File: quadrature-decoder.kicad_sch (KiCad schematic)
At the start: 6 parts, among them J1 Screw_Terminal_01x05, J2 Conn_02x20_Counter_Clockwise, U1 4013, U2 4029, U3 4029, U4 4029

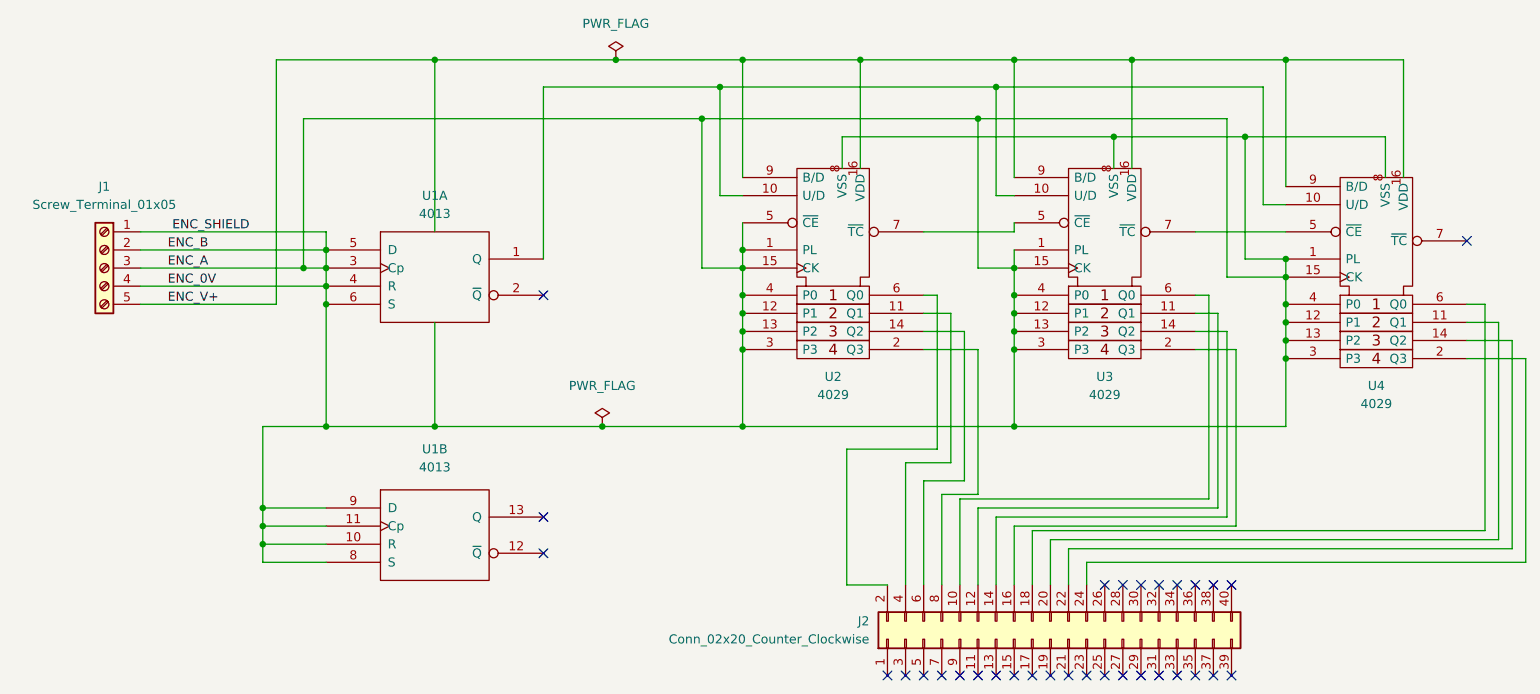
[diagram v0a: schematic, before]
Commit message: Improve routing and component positioning; add capacitors
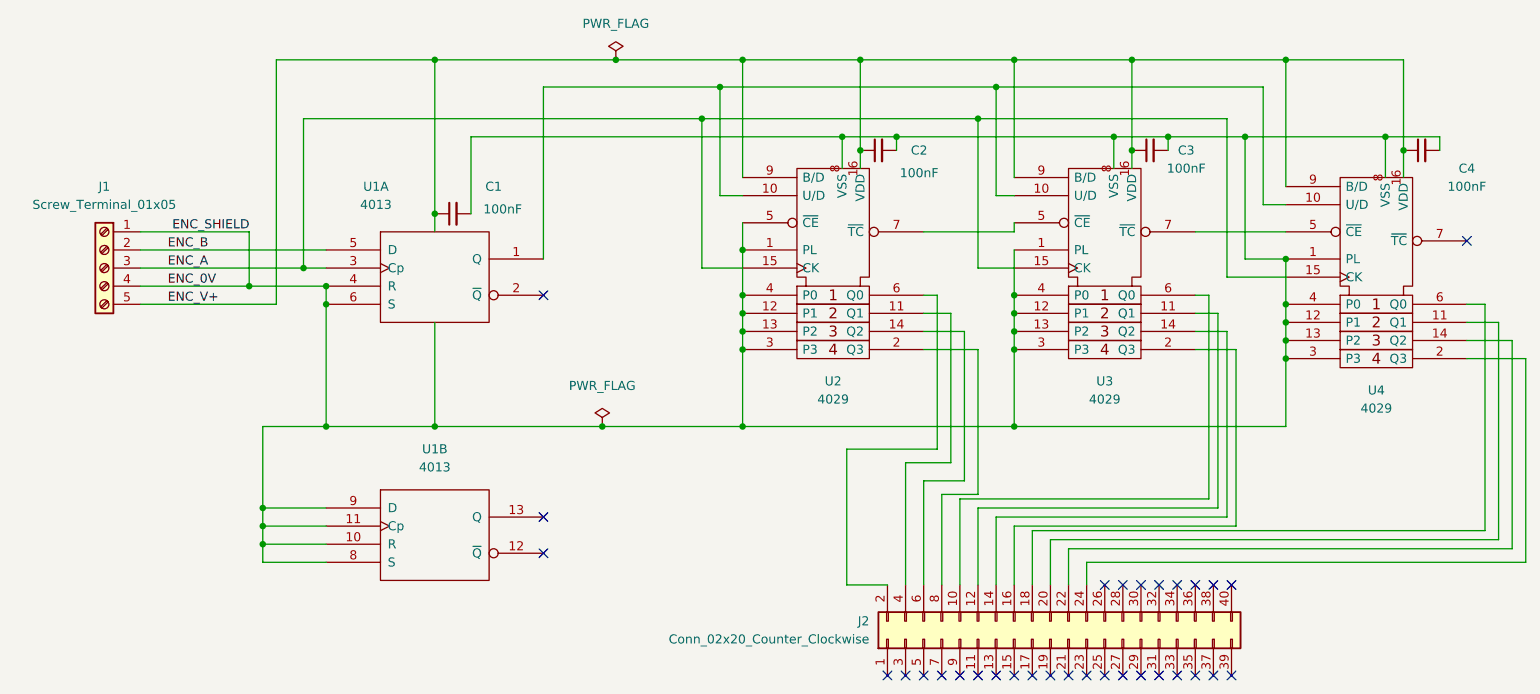
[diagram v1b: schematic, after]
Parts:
- added C1, C2, C3, C4: 100nF, Capacitor_THT:C_Axial_L3.8mm_D2.6mm_P7.50mm_Horizontal, symbol Device:C_Small
- U1: footprint Package_DIP:DIP-14_W7.62mm_LongPads -> Package_DIP:DIP-14_W7.62mm_Socket_LongPads
- U2, U3, U4: footprint Package_DIP:DIP-16_W7.62mm_LongPads -> Package_DIP:DIP-16_W7.62mm_Socket_LongPads
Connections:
- net Vdd: now also C1.1, C2.1, C3.1, C4.1
- net Vss: now also C1.2, C2.2, C3.2, C4.2; no longer J1.2 (Pin_2), J1.3 (Pin_3), U1.3 (Cp), U1.5 (D), U2.15 (CK), U3.15 (CK), U4.15 (CK)
- new net ENC_A: J1.3 (Pin_3), U1.3 (Cp), U2.15 (CK), U3.15 (CK), U4.15 (CK)
- new net ENC_B: J1.2 (Pin_2), U1.5 (D)
